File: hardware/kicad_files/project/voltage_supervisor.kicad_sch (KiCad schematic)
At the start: 2 parts, among them U8 MCP1319MT-29LE-OT

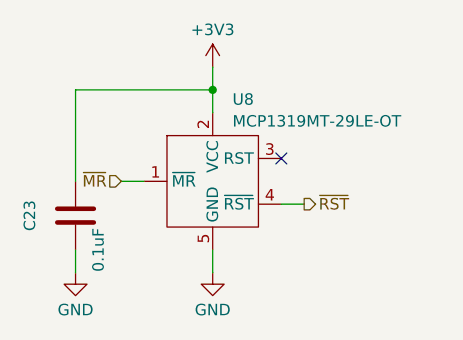
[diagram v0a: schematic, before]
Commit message: feat: update to 0.2
feat: add pin sockets compatible to the Pmod interface

feat: add a power switch and an overcurrent protection circuit, including a fault status LED and a solder bridge

fix: remove the clock jumpers and directly connect the second output clock to the user clock input

misc: remove the jumpers from io 36 and 37 to the bitbang inputs, add bitbang pins to the UART connector

cosmetic: make the PCB edges round
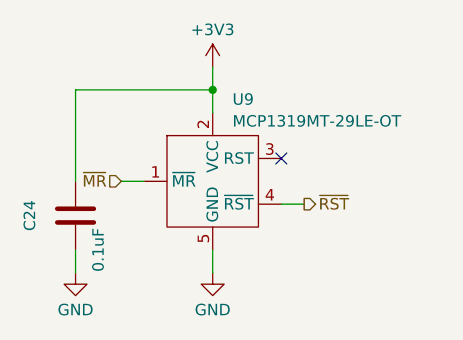
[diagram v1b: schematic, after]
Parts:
- renumbered C23 to C24, U8 to U9
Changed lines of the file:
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@@
 		(title "Voltage Supervisor")
 		(date "2024-05-30")
-		(rev "0.1.1")
+		(rev "0.2.0")
 	)
 	(junction
@@
 		(dnp no)
 		(fields_autoplaced yes)
-		(property "Reference" "#PWR066"
+		(property "Reference" "#PWR73"
 			(at 127 91.44 0)
 			(effects
@@
 			(project "FABulous_board"
 				(path "/5664f05e-a3ef-4177-8026-c4580fa32c71/61abf8ce-9ba2-4995-9a57-37e178bb3e97"
-					(reference "#PWR066")
+					(reference "#PWR73")
 					(unit 1)
 				)
@@
 		(on_board yes)
 		(dnp no)
-		(property "Reference" "C23"
+		(property "Reference" "C24"
 			(at 106.68 104.14 90)
 			(effects
@@
 			(project "FABulous_board"
 				(path "/5664f05e-a3ef-4177-8026-c4580fa32c71/61abf8ce-9ba2-4995-9a57-37e178bb3e97"
-					(reference "C23")
+					(reference "C24")
 					(unit 1)
 				)
@@
 		(dnp no)
 		(fields_autoplaced yes)
-		(property "Reference" "U8"
+		(property "Reference" "U9"
 			(at 129.1941 91.2325 0)
 			(effects
@@
 			(project "FABulous_board"
 				(path "/5664f05e-a3ef-4177-8026-c4580fa32c71/61abf8ce-9ba2-4995-9a57-37e178bb3e97"
-					(reference "U8")
+					(reference "U9")
 					(unit 1)
 				)
@@
 		(dnp no)
 		(fields_autoplaced yes)
-		(property "Reference" "#PWR067"
+		(property "Reference" "#PWR74"
 			(at 127 116.84 0)
 			(effects
@@
 			(project "FABulous_board"
 				(path "/5664f05e-a3ef-4177-8026-c4580fa32c71/61abf8ce-9ba2-4995-9a57-37e178bb3e97"
-					(reference "#PWR067")
+					(reference "#PWR74")
 					(unit 1)
 				)
@@
 		(dnp no)
 		(fields_autoplaced yes)
-		(property "Reference" "#PWR065"
+		(property "Reference" "#PWR72"
 			(at 111.76 116.84 0)
 			(effects
@@
 			(project "FABulous_board"
 				(path "/5664f05e-a3ef-4177-8026-c4580fa32c71/61abf8ce-9ba2-4995-9a57-37e178bb3e97"
-					(reference "#PWR065")
+					(reference "#PWR72")
 					(unit 1)
 				)
